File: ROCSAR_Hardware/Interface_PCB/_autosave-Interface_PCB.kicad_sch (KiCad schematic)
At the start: 35 parts, among them J1 Remove Before Flight, J2 USB_A, J3 USB_A, U1 TEN 60-2422N, U2 LM2576-5.0WU, U3 LM2576-5.0WU, U4 LM2576-5.0WU, U5 LM2576-5.0WU

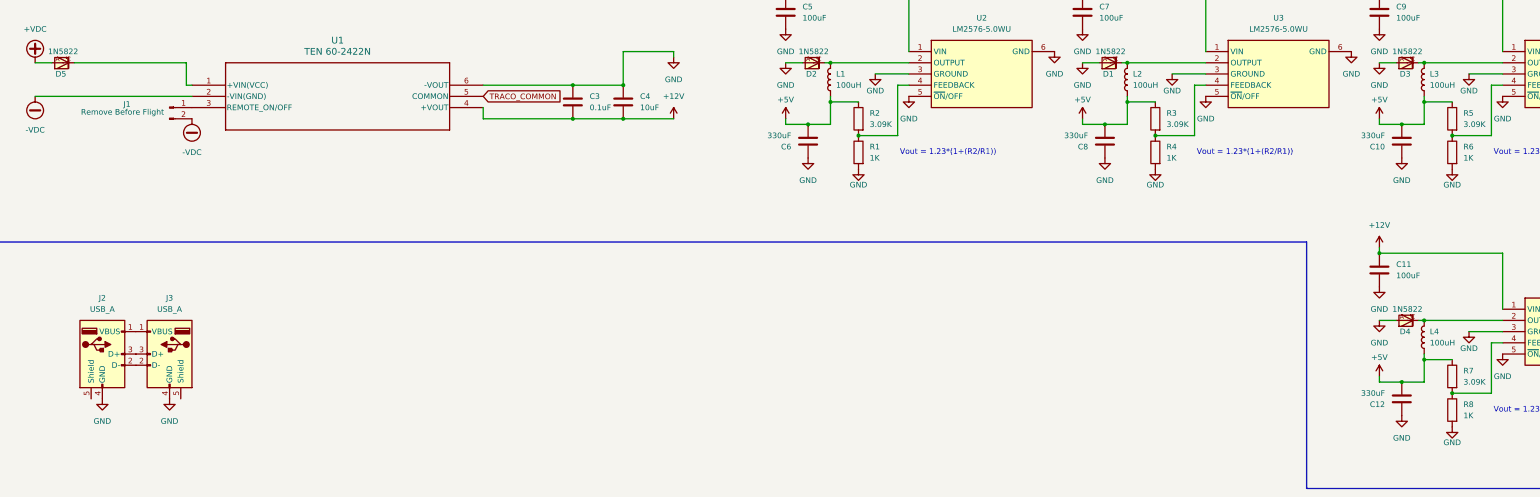
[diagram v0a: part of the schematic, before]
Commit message: Continuation of the development of the interface pcb
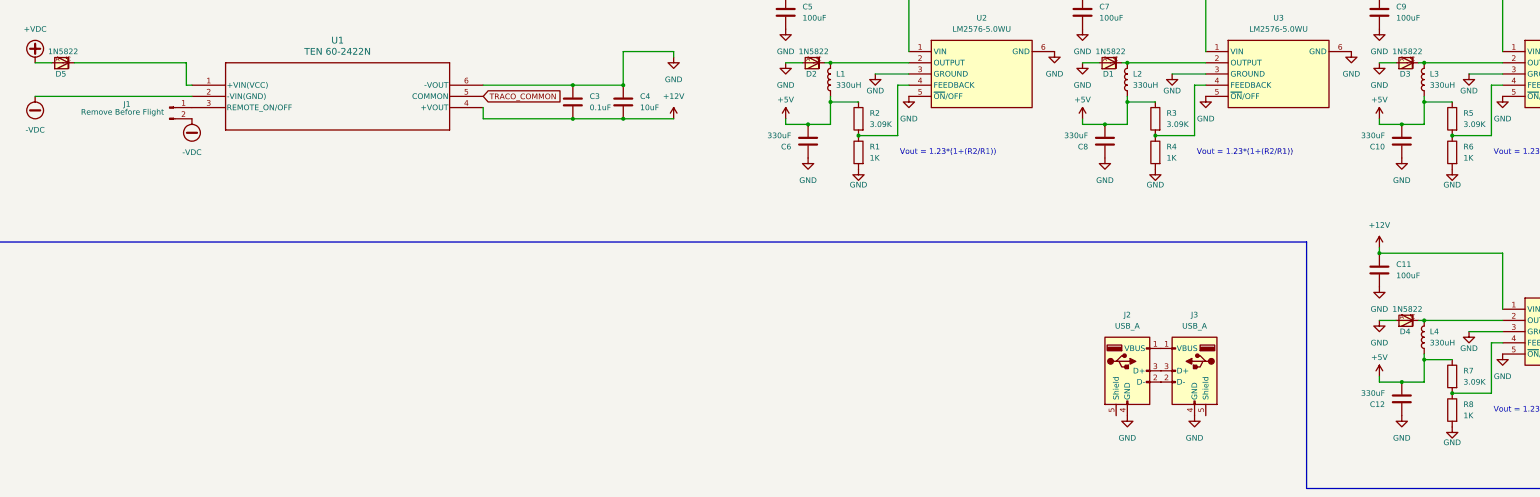
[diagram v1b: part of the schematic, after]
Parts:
- L1, L2, L3, L4: value 100uH -> 330uH; footprint (none) -> SRR1050HA-331Y:INDPM102100X510N
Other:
- moved on the sheet: J2, J3
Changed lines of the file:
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@@
 			)
 		)
-		(property "Value" "100uH"
+		(property "Value" "330uH"
 			(at 346.71 48.2599 0)
 			(effects
@@
 			)
 		)
-		(property "Footprint" ""
+		(property "Footprint" "SRR1050HA-331Y:INDPM102100X510N"
 			(at 345.44 46.99 0)
 			(effects
@@
 			)
 		)
-		(property "Value" "100uH"
+		(property "Value" "330uH"
 			(at 279.4 48.2599 0)
 			(effects
@@
 			)
 		)
-		(property "Footprint" ""
+		(property "Footprint" "SRR1050HA-331Y:INDPM102100X510N"
 			(at 278.13 46.99 0)
 			(effects
@@
 	(symbol
 		(lib_id "Connector:USB_A")
-		(at 60.96 109.22 0)
+		(at 293.37 113.03 0)
 		(mirror y)
 		(unit 1)
@@
 		(dnp no)
 		(property "Reference" "J3"
-			(at 60.96 96.52 0)
+			(at 293.37 100.33 0)
 			(effects
 				(font
@@
 		)
 		(property "Value" "USB_A"
-			(at 60.96 99.06 0)
+			(at 293.37 102.87 0)
 			(effects
 				(font
@@
 		)
 		(property "Footprint" "Connector_USB:USB_A_Molex_67643_Horizontal"
-			(at 57.15 110.49 0)
+			(at 289.56 114.3 0)
 			(effects
 				(font
@@
 		)
 		(property "Datasheet" "~"
-			(at 57.15 110.49 0)
+			(at 289.56 114.3 0)
 			(effects
 				(font
@@
 		)
 		(property "Description" "USB Type A connector"
-			(at 60.96 109.22 0)
+			(at 293.37 113.03 0)
 			(effects
 				(font
@@
 	(symbol
 		(lib_id "power:GND")
-		(at 60.96 119.38 0)
+		(at 293.37 123.19 0)
 		(unit 1)
 		(exclude_from_sim no)
@@
 		(fields_autoplaced yes)
 		(property "Reference" "#PWR043"
-			(at 60.96 125.73 0)
+			(at 293.37 129.54 0)
 			(effects
 				(font
@@
 		)
 		(property "Value" "GND"
-			(at 60.96 124.46 0)
+			(at 293.37 128.27 0)
 			(effects
 				(font
@@
 		)
 		(property "Footprint" ""
-			(at 60.96 119.38 0)
+			(at 293.37 123.19 0)
 			(effects
 				(font
@@
 		)
 		(property "Datasheet" ""
-			(at 60.96 119.38 0)
+			(at 293.37 123.19 0)
 			(effects
 				(font
@@
 		)
 		(property "Description" "Power symbol creates a global label with name \"GND\" , ground"
-			(at 60.96 119.38 0)
+			(at 293.37 123.19 0)
 			(effects
 				(font
@@
 			)
 		)
-		(property "Value" "100uH"
+		(property "Value" "330uH"
 			(at 212.09 48.2599 0)
 			(effects
@@
 			)
 		)
-		(property "Footprint" ""
+		(property "Footprint" "SRR1050HA-331Y:INDPM102100X510N"
 			(at 210.82 46.99 0)
 			(effects
@@
 	(symbol
 		(lib_id "Connector:USB_A")
-		(at 45.72 109.22 0)
+		(at 278.13 113.03 0)
 		(unit 1)
 		(exclude_from_sim no)
@@
 		(fields_autoplaced yes)
 		(property "Reference" "J2"
-			(at 45.72 96.52 0)
+			(at 278.13 100.33 0)
 			(effects
 				(font
@@
 		)
 		(property "Value" "USB_A"
-			(at 45.72 99.06 0)
+			(at 278.13 102.87 0)
 			(effects
 				(font
@@
 		)
 		(property "Footprint" "Connector_USB:USB_A_Molex_67643_Horizontal"
-			(at 49.53 110.49 0)
+			(at 281.94 114.3 0)
 			(effects
 				(font
@@
 		)
 		(property "Datasheet" "~"
-			(at 49.53 110.49 0)
+			(at 281.94 114.3 0)
 			(effects
 				(font
@@
 		)
 		(property "Description" "USB Type A connector"
-			(at 45.72 109.22 0)
+			(at 278.13 113.03 0)
 			(effects
 				(font
@@
 			)
 		)
-		(property "Value" "100uH"
+		(property "Value" "330uH"
 			(at 346.71 106.6799 0)
 			(effects
@@
 			)
 		)
-		(property "Footprint" ""
+		(property "Footprint" "SRR1050HA-331Y:INDPM102100X510N"
 			(at 345.44 105.41 0)
 			(effects
@@
 	(symbol
 		(lib_id "power:GND")
-		(at 45.72 119.38 0)
+		(at 278.13 123.19 0)
 		(unit 1)
 		(exclude_from_sim no)
@@
 		(fields_autoplaced yes)
 		(property "Reference" "#PWR042"
-			(at 45.72 125.73 0)
+			(at 278.13 129.54 0)
 			(effects
 				(font
@@
 		)
 		(property "Value" "GND"
-			(at 45.72 124.46 0)
+			(at 278.13 128.27 0)
 			(effects
 				(font
@@
 		)
 		(property "Footprint" ""
-			(at 45.72 119.38 0)
+			(at 278.13 123.19 0)
 			(effects
 				(font
@@
 		)
 		(property "Datasheet" ""
-			(at 45.72 119.38 0)
+			(at 278.13 123.19 0)
 			(effects
 				(font
@@
 		)
 		(property "Description" "Power symbol creates a global label with name \"GND\" , ground"
-			(at 45.72 119.38 0)
+			(at 278.13 123.19 0)
 			(effects
 				(font
